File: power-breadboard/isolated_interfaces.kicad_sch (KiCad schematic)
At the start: 6 parts, among them U17 RFM-0505S, U19 RFM-0505S

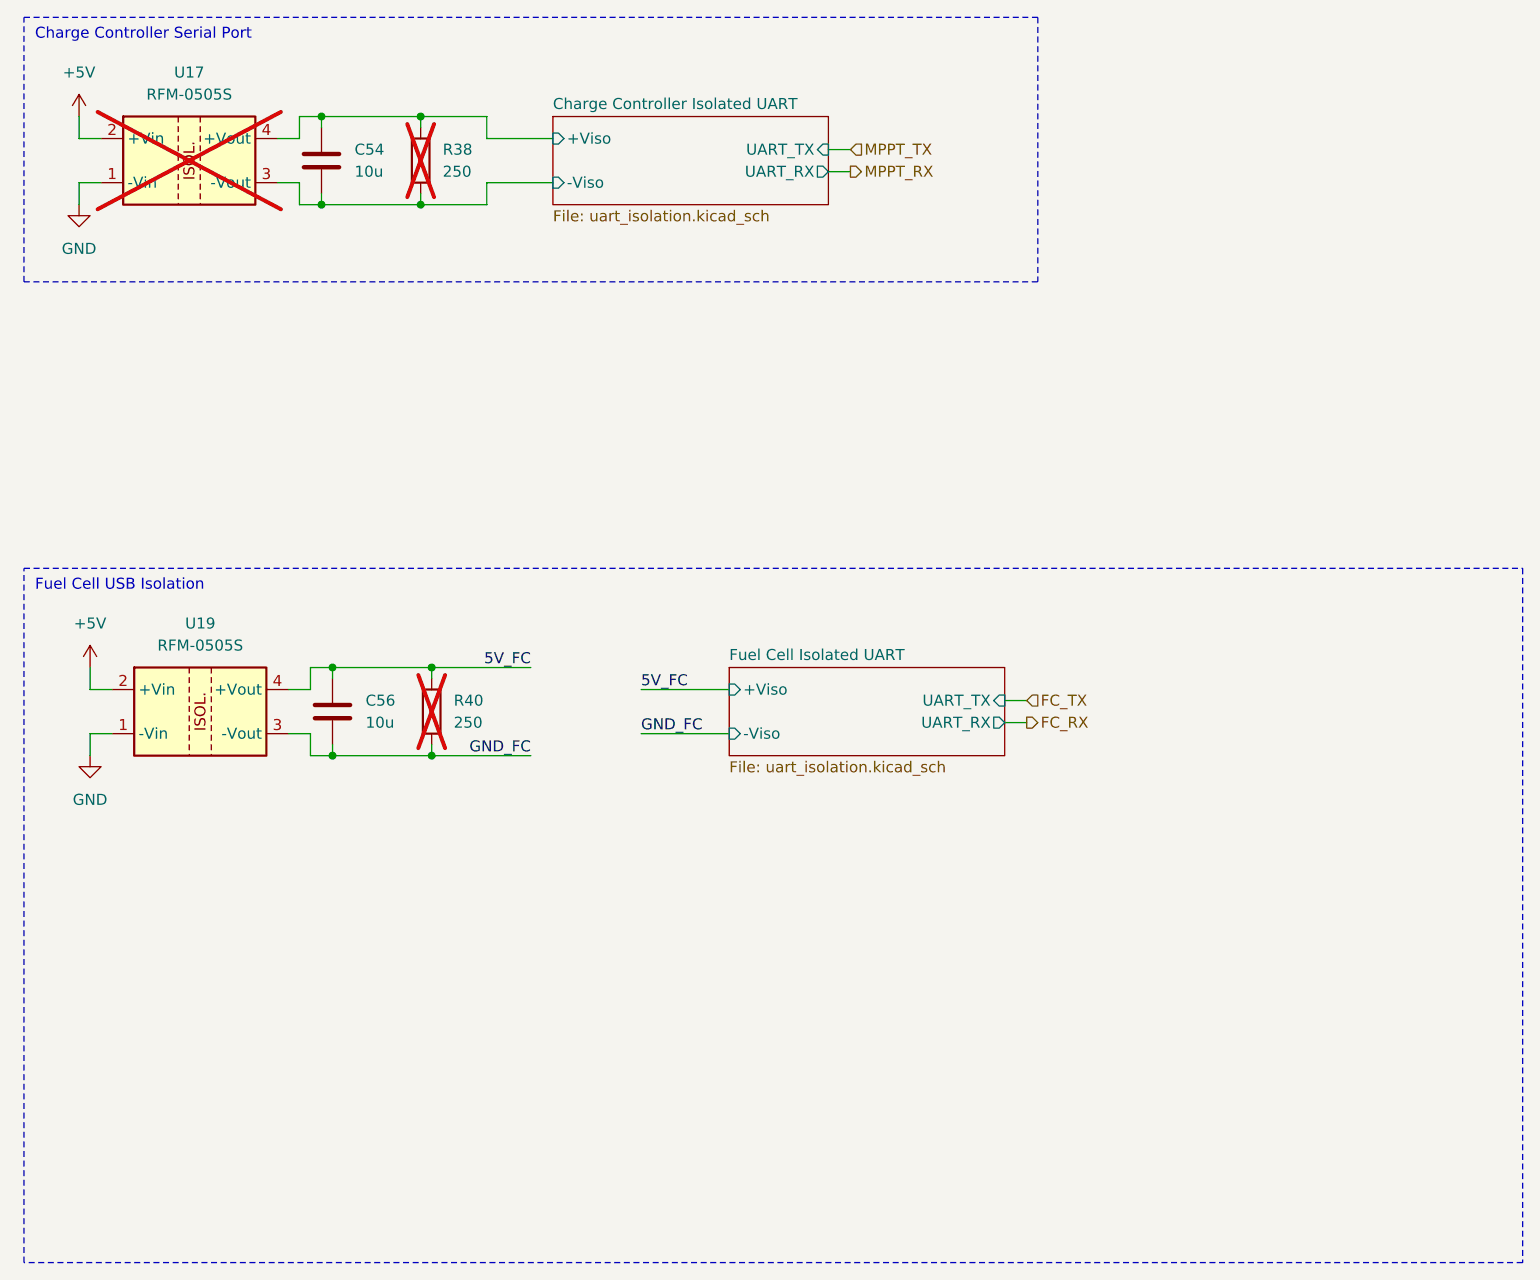
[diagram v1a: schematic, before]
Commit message: power-breadboard: finish isolated interfaces
Replaced UART isolators with discrete optocouplers.
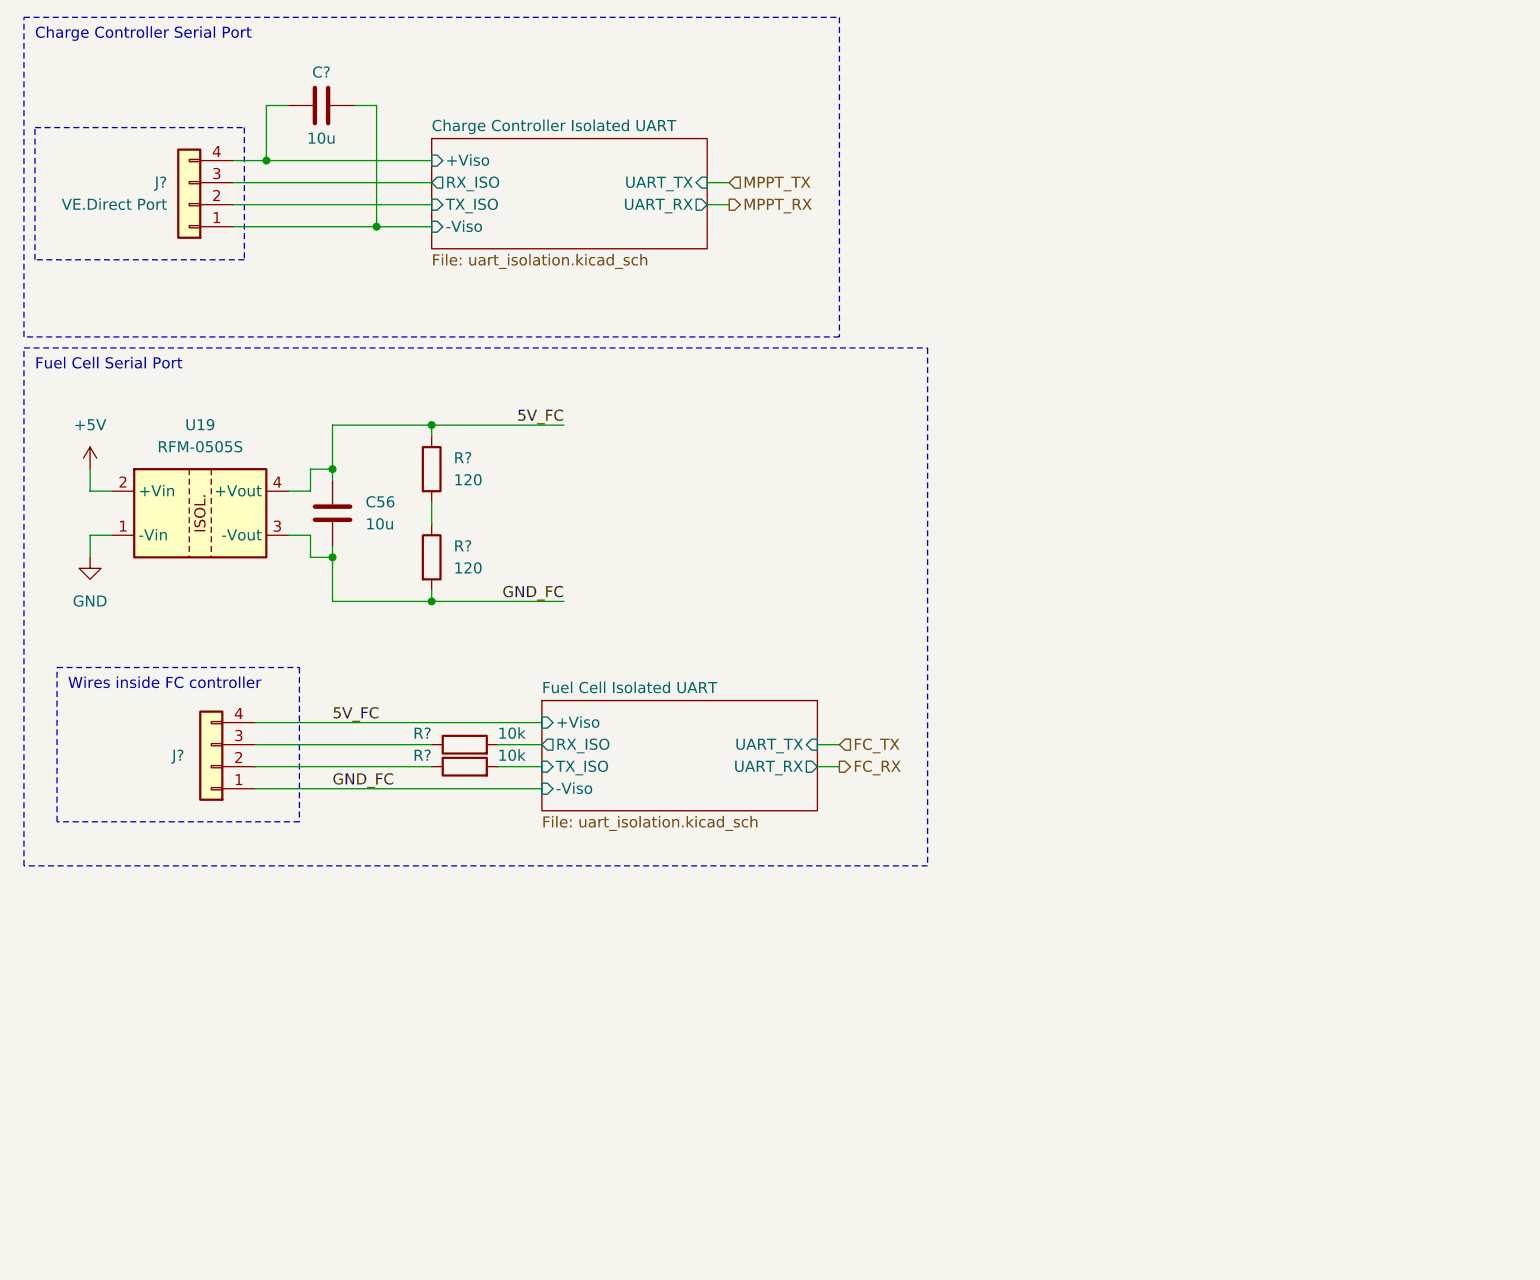
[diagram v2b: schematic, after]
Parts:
- removed C54: 10u, Capacitor_SMD:C_1206_3216Metric_Pad1.33x1.80mm_HandSolder, symbol Device:C
- removed R38, R40: 250, Resistor_THT:R_Axial_DIN0309_L9.0mm_D3.2mm_P12.70mm_Horizontal, symbol Device:R
- removed U17: RFM-0505S, Exocet:RECOM_SIP-4, symbol Exocet:RFM-0505S
- added C?: 10u, symbol Device:C
- added J?: Conn_01x04, symbol Connector_Generic:Conn_01x04
- added J?: VE.Direct Port, symbol Connector_Generic:Conn_01x04
- added R? (x2): 10k, symbol Device:R
- added R? (x2): 120, symbol Device:R
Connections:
- net 5V_FC: now also J?.4 (Pin_4), R?.1
- net Charge Controller Isolated UART/+Viso: now also C?.1, J?.4 (Pin_4)
- net Charge Controller Isolated UART/-Viso: now also C?.2, J?.1 (Pin_1)
- net GND_FC: now also J?.1 (Pin_1), R?.2
- new net: J?.2 (Pin_2), R?.1
- new net: R?.1, R?.2
- new net: J?.3 (Pin_3), R?.1
- new net Charge Controller Isolated UART/RX_ISO: J?.3 (Pin_3)
- new net Charge Controller Isolated UART/TX_ISO: J?.2 (Pin_2)
- new net Fuel Cell Isolated UART/RX_ISO: R?.2
- new net Fuel Cell Isolated UART/TX_ISO: R?.2
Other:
- sheet Charge Controller Isolated UART ports: added RX_ISO, TX_ISO; removed none
- sheet Fuel Cell Isolated UART ports: added RX_ISO, TX_ISO; removed none
- note added: "Fuel Cell Serial Port"
- note added: "Wires inside FC controller"
- note removed: "Fuel Cell USB Isolation"
- moved on the sheet: C56, U19
